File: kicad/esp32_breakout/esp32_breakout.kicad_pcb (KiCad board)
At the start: 2 copper layers, 73.8 x 33.1 mm, 26 parts, among them J1 JST B5B-PH-K-S, J10 JST B6B-PH-K-S, J2 JST B5B-PH-K-S, J3 JST B7B-PH-K-S, J4 XT30U-M, J5 HDR 8p M VERT 2.54mm, J6 JST B5B-ZR, J9 JST B6B-PH-K-S, SW1 SS12D10, U1 ESP32 DEV KIT Module 30-pin, U2 LM2596 Module

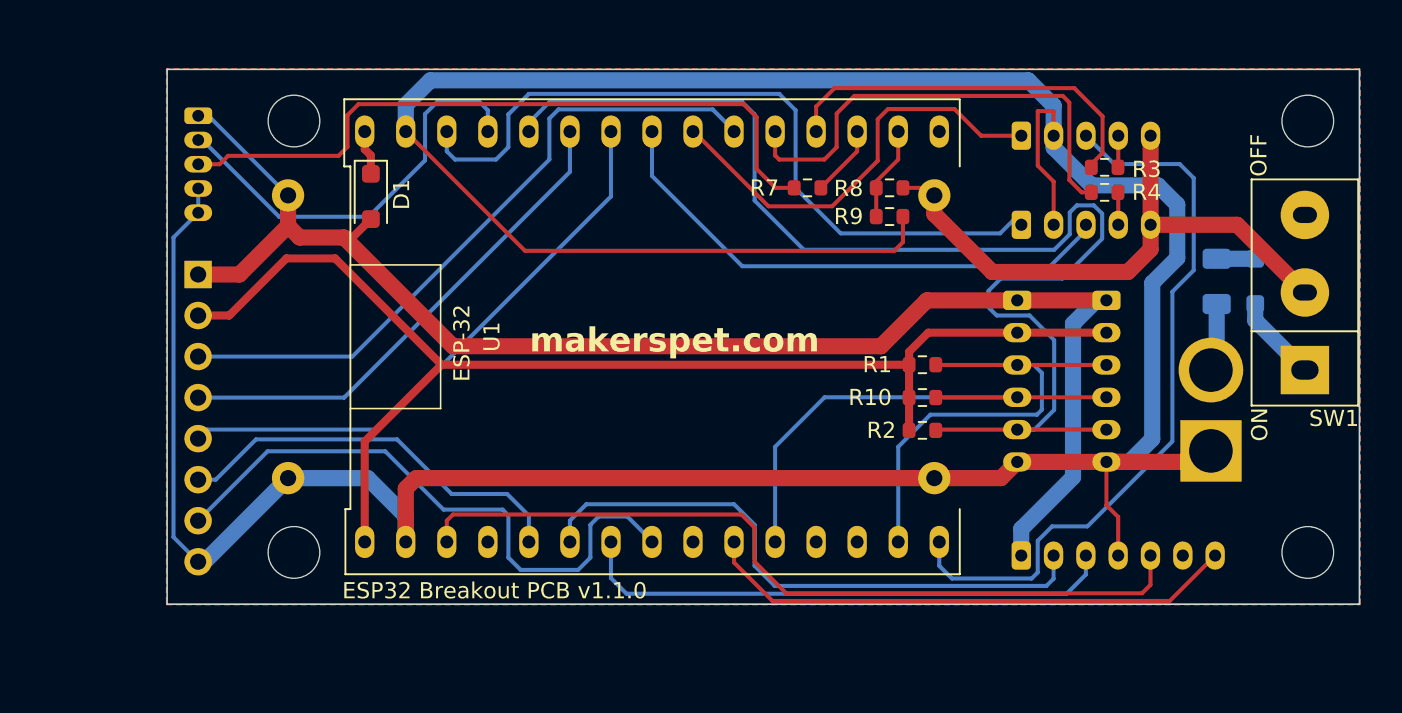
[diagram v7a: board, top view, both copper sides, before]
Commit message: Single GPIO header
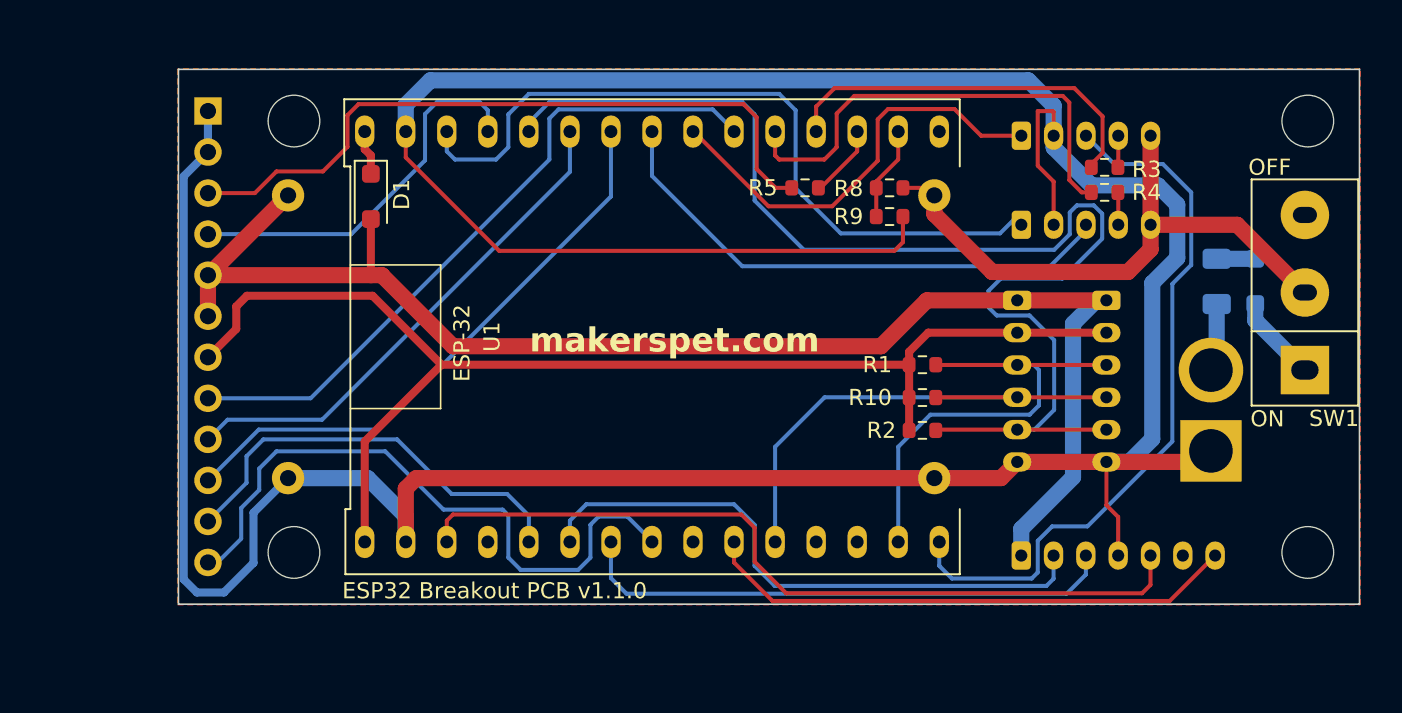
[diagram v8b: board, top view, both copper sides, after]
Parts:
- removed J6: JST B5B-ZR, Makerspet:JST_ZH_B5B-ZR_1x05_P1.50mm_Vertical
- removed R7: 10k, Resistor_SMD:R_0603_1608Metric
- added R5: 10k, Resistor_SMD:R_0603_1608Metric, F.Cu at (161.1, 87.1)
- J5: value HDR 8p M VERT 2.54mm -> HDR M VERT 12p 2.54mm; footprint Connector_PinHeader_2.54mm:PinHeader_1x08_P2.54mm_Vertical -> Connector_PinSocket_2.54mm:PinSocket_1x12_P2.54mm_Vertical
- moved J5 10.1 mm to (124.2, 82.3)
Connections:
- J5 pad 1: +5V -> GND
- J5 pad 2: +3V3 -> GND
- J5 pad 3: /GPIO32_TOUCH -> Net-(J5-Pin_3)
- J5 pad 4: /GPIO27_TOUCH -> /GPIO12_OUT_STRAP
- J5 pad 5: /GPIO26_TOUCH -> +5V
- J5 pad 6: /GPIO4_TOUCH -> +5V
- J5 pad 7: /GPIO5_BOOT_STRAP -> +3V3
- J5 pad 8: GND -> /GPIO32_TOUCH
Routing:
- net Net-(J6-Pin_3): track 43.6 -> 0.00 mm
- net Net-(J5-Pin_3): track 0.00 -> 43.6 mm
- net GND: track 221.6 -> 232.2 mm
- net /GPIO5_BOOT_STRAP: track 37.6 -> 40.0 mm
- net /GPIO12_OUT_STRAP: track 26.0 -> 23.9 mm
- net +5V: track 91.7 -> 90.0 mm
- net /GPIO4_TOUCH: track 25.1 -> 26.5 mm
- net /MOT_CW_LEFT: track 45.5 -> 44.8 mm
- net +3V3: track 78.7 -> 78.0 mm
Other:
- board size 73.8 x 33.1 mm -> 73.1 x 33.1 mm
